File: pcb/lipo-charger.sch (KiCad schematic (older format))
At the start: 15 parts, among them J101 Barrel_Jack, J102 Conn_01x04, J103 Conn_01x03, J104 Conn_01x03, P101 Polarity, P102 Outline, P103 OSHW, U101 LM317L_TO92

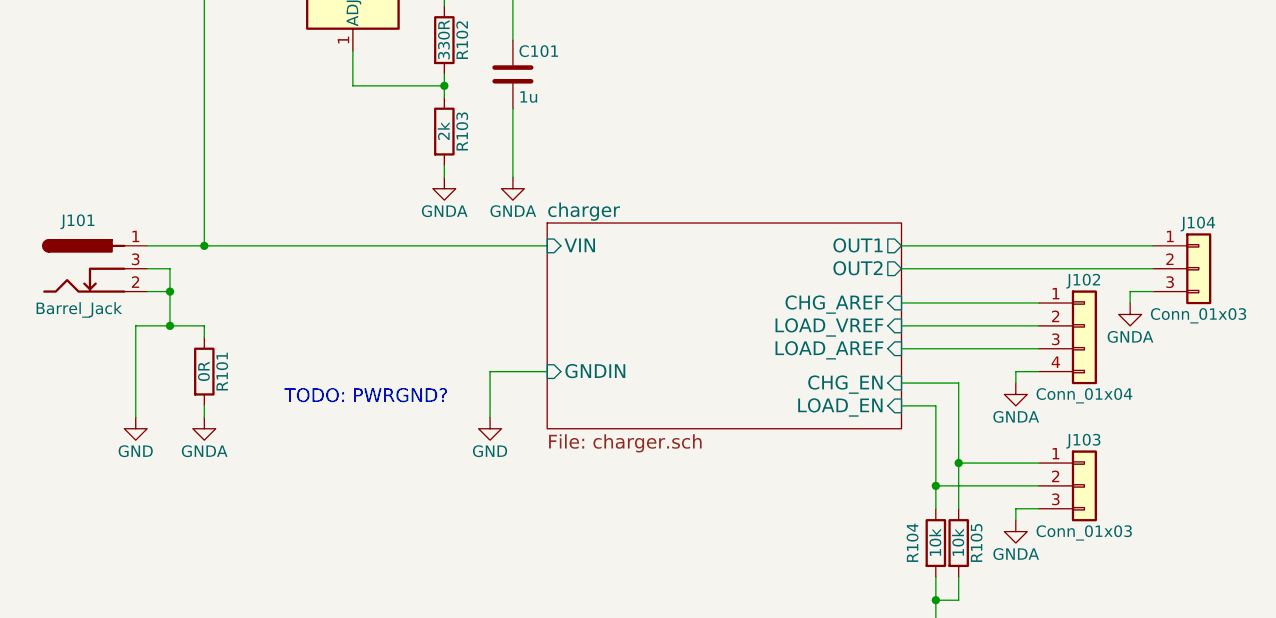
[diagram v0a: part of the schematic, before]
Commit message: Fix ERC/DRC errors for first prototype
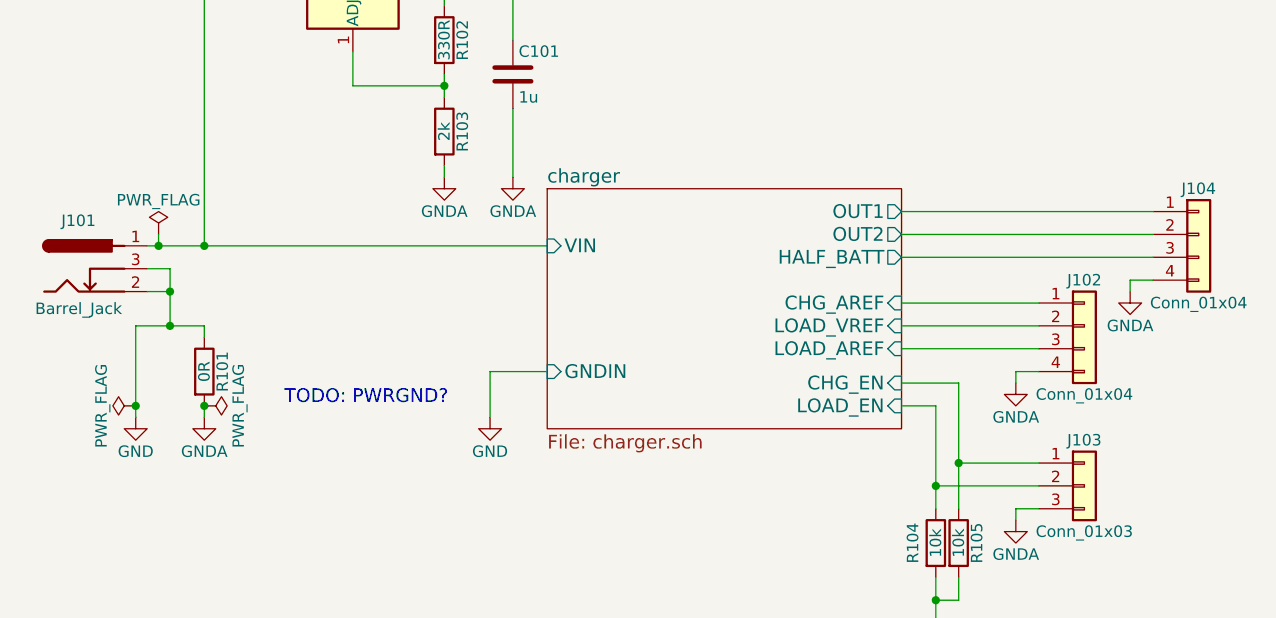
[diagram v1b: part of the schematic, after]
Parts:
- removed J104: Conn_01x03, Pin_Headers:Pin_Header_Straight_1x03_Pitch2.54mm, symbol Conn_01x03
- added J104: Conn_01x04, Pin_Headers:Pin_Header_Straight_1x04_Pitch2.54mm, symbol Conn_01x04
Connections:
- net GNDA: now also J104.4 (Pin_4)
- net charger/OUT1: now also J104.1 (Pin_1)
- net charger/OUT2: now also J104.2 (Pin_2)
- new net charger/HALF_BATT: J104.3 (Pin_3)
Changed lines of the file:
@@
 $EndComp
 $Sheet
-S 5300 2000 1550 900
+S 5300 1850 1550 1050
 U 5A337ADE
 F0 "charger" 60
@@
 F6 "LOAD_VREF" I R 6850 2450 60
 F7 "GNDIN" I L 5300 2650 60
-F8 "OUT1" O R 6850 2100 60
-F9 "OUT2" O R 6850 2200 60
+F8 "OUT1" O R 6850 1950 60
+F9 "OUT2" O R 6850 2050 60
 F10 "LOAD_EN" I R 6850 2800 60
+F11 "HALF_BATT" O R 6850 2150 60
 $EndSheet
 $Comp
@@
 Wire Wire Line
 	5150 900  5150 1200
-$Comp
-L Conn_01x03 J104
-U 1 1 5A3CE784
-P 8150 2200
-F 0 "J104" H 8150 2400 50  0000 C CNN
-F 1 "Conn_01x03" H 8150 2000 50  0000 C CNN
-F 2 "Pin_Headers:Pin_Header_Straight_1x03_Pitch2.54mm" H 8150 2200 50  0001 C CNN
-F 3 "" H 8150 2200 50  0001 C CNN
-	1    8150 2200
-	1    0    0    -1
-$EndComp
-Wire Wire Line
-	7950 2100 6850 2100
-Wire Wire Line
-	6850 2200 7950 2200
+Wire Wire Line
+	7950 1950 6850 1950
+Wire Wire Line
+	6850 2050 7950 2050
 $Comp
 L GNDA #PWR06
 U 1 1 5A3CE8B0
-P 7850 2350
-F 0 "#PWR06" H 7850 2100 50  0001 C CNN
-F 1 "GNDA" H 7850 2200 50  0000 C CNN
-F 2 "" H 7850 2350 50  0001 C CNN
-F 3 "" H 7850 2350 50  0001 C CNN
-	1    7850 2350
-	1    0    0    -1
-$EndComp
-Wire Wire Line
-	7950 2300 7850 2300
-Wire Wire Line
-	7850 2300 7850 2350
+P 7850 2300
+F 0 "#PWR06" H 7850 2050 50  0001 C CNN
+F 1 "GNDA" H 7850 2150 50  0000 C CNN
+F 2 "" H 7850 2300 50  0001 C CNN
+F 3 "" H 7850 2300 50  0001 C CNN
+	1    7850 2300
+	1    0    0    -1
+$EndComp
+Wire Wire Line
+	7950 2250 7850 2250
+Wire Wire Line
+	7850 2250 7850 2300
 $Comp
 L Conn_01x04 J102
@@
 	1    0    0    -1
 $EndComp
+$Comp
+L Conn_01x04 J104
+U 1 1 5A3D7236
+P 8150 2050
+F 0 "J104" H 8150 2250 50  0000 C CNN
+F 1 "Conn_01x04" H 8150 1750 50  0000 C CNN
+F 2 "Pin_Headers:Pin_Header_Straight_1x04_Pitch2.54mm" H 8150 2050 50  0001 C CNN
+F 3 "" H 8150 2050 50  0001 C CNN
+	1    8150 2050
+	1    0    0    -1
+$EndComp
+Wire Wire Line
+	6850 2150 7950 2150
+$Comp
+L PWR_FLAG #FLG011
+U 1 1 5A3D7A81
+P 3500 2800
+F 0 "#FLG011" H 3500 2875 50  0001 C CNN
+F 1 "PWR_FLAG" H 3500 2950 50  0000 C CNN
+F 2 "" H 3500 2800 50  0001 C CNN
+F 3 "" H 3500 2800 50  0001 C CNN
+	1    3500 2800
+	0    -1   -1   0
+$EndComp
+$Comp
+L PWR_FLAG #FLG012
+U 1 1 5A3D7AFC
+P 3800 2800
+F 0 "#FLG012" H 3800 2875 50  0001 C CNN
+F 1 "PWR_FLAG" H 3800 2950 50  0000 C CNN
+F 2 "" H 3800 2800 50  0001 C CNN
+F 3 "" H 3800 2800 50  0001 C CNN
+	1    3800 2800
+	0    1    1    0
+$EndComp
+Connection ~ 3800 2800
+Connection ~ 3500 2800
+$Comp
+L PWR_FLAG #FLG013
+U 1 1 5A3D7BDD
+P 3600 2050
+F 0 "#FLG013" H 3600 2125 50  0001 C CNN
+F 1 "PWR_FLAG" H 3600 2200 50  0000 C CNN
+F 2 "" H 3600 2050 50  0001 C CNN
+F 3 "" H 3600 2050 50  0001 C CNN
+	1    3600 2050
+	1    0    0    -1
+$EndComp
+Wire Wire Line
+	3600 2050 3600 2100
+Connection ~ 3600 2100
 $EndSCHEMATC

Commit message: Massive rework, fully routed
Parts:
- removed C101: 1u, Capacitors_SMD_Round:C_0805, symbol C
- removed J101: Barrel_Jack, Connectors:Barrel_Jack_CUI_PJ-102AH, symbol Barrel_Jack
- removed J103: Conn_01x03, Pin_Headers:Pin_Header_Straight_1x03_Pitch2.54mm, symbol Conn_01x03
- removed J104: Conn_01x04, Pin_Headers:Pin_Header_Straight_1x04_Pitch2.54mm, symbol Conn_01x04
- removed P101: Polarity, Polarity_Symbols:Polarity_Center_Positive_3mm_SilkScreen, symbol SYMBOL
- removed R102: 330R, Resistors_SMD:R_0603_HandSoldering, symbol R
- removed R103: 2k, Resistors_SMD:R_0603_HandSoldering, symbol R
- removed R104, R105: 10k, Resistors_SMD:R_0603_HandSoldering, symbol R
- removed TP101: TEST, Measurement_Points:Measurement_Point_Round-SMD-Pad_Small, symbol TEST
- removed U101: LM317L_TO92, TO_SOT_Packages_THT:TO-92_Inline_Narrow_Oval, symbol LM317L_TO92
- added J101, J103: Conn_01x04, Connectors_Molex:Molex_KK-6410-04_04x2.54mm_Straight, symbol Conn_01x04
- added J104: Conn_01x03, Connectors_Molex:Molex_KK-6410-03_03x2.54mm_Straight, symbol Conn_01x03
- added P? (x2): Fid, Fiducials:Fiducial_1mm_Dia_2.54mm_Outer_CopperTop, symbol SYMBOL
- J102: footprint Pin_Headers:Pin_Header_Straight_1x04_Pitch2.54mm -> Connectors_Molex:Molex_KK-6410-04_04x2.54mm_Straight
- R101: value 0R -> 100R
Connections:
- net +9VA: now also J102.1 (Pin_1)
- net GNDA: now also J102.2 (Pin_2), J101.4 (Pin_4), J103.4 (Pin_4), J104.3 (Pin_3); no longer J102.4 (Pin_4)
- net charger/CHG_AREF: now also J101.2 (Pin_2); no longer J102.1 (Pin_1)
- net charger/CHG_EN: now also J101.1 (Pin_1)
- net charger/LOAD_AREF: now also J103.3 (Pin_3); no longer J102.3 (Pin_3)
- net charger/LOAD_EN: now also J103.1 (Pin_1)
- net charger/LOAD_VREF: now also J103.2 (Pin_2); no longer J102.2 (Pin_2)
- net charger/OUT1: now also J104.1 (Pin_1)
- net charger/OUT2: now also J104.2 (Pin_2)
- net charger/VIN: now also J102.3 (Pin_3)
- net GND renamed charger/GNDIN
- net charger/GNDIN: now also J102.4 (Pin_4)
- new net charger/MASTER_EN: J101.3 (Pin_3)
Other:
- note added: "Note: R101 is optional\ntie between grounds"
- note added: "This is a dev board which might\nbecome a module in a larger\ncharger apparatus."
- note removed: "TODO: PWRGND?"

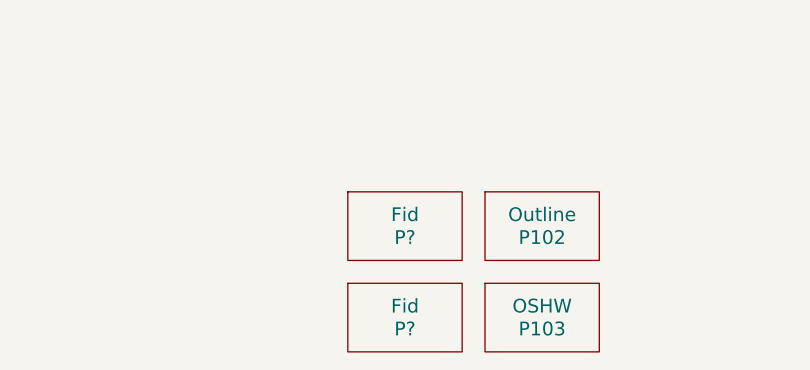
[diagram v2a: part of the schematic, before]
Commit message: Rename some nets, ordered.
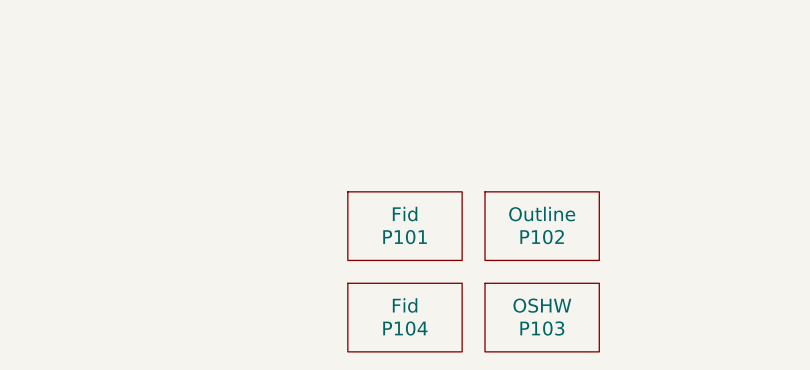
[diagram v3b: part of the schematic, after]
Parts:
- gave numbers to parts that had none: 2
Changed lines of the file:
@@
 	5100 2800 5100 3250
 $Comp
-L +9VA #PWR01
+L +9VA #PWR101
 U 1 1 5A473903
 P 5100 2800
-F 0 "#PWR01" H 5100 2675 50  0001 C CNN
+F 0 "#PWR101" H 5100 2675 50  0001 C CNN
 F 1 "+9VA" H 5100 2950 50  0000 C CNN
 F 2 "" H 5100 2800 50  0001 C CNN
@@
 $EndComp
 $Comp
-L GNDA #PWR02
+L GNDA #PWR103
 U 1 1 5A473953
 P 5600 3100
-F 0 "#PWR02" H 5600 2850 50  0001 C CNN
+F 0 "#PWR103" H 5600 2850 50  0001 C CNN
 F 1 "GNDA" H 5600 2950 50  0000 C CNN
 F 2 "" H 5600 3100 50  0001 C CNN
@@
 $EndComp
 $Comp
-L GNDA #PWR03
+L GNDA #PWR102
 U 1 1 5A4739A7
 P 5250 4600
-F 0 "#PWR03" H 5250 4350 50  0001 C CNN
+F 0 "#PWR102" H 5250 4350 50  0001 C CNN
 F 1 "GNDA" H 5250 4450 50  0000 C CNN
 F 2 "" H 5250 4600 50  0001 C CNN
@@
 $EndComp
 $Comp
-L PWR_FLAG #FLG04
+L PWR_FLAG #FLG102
 U 1 1 5A473E6C
 P 5550 3050
-F 0 "#FLG04" H 5550 3125 50  0001 C CNN
+F 0 "#FLG102" H 5550 3125 50  0001 C CNN
 F 1 "PWR_FLAG" H 5550 3200 50  0000 C CNN
 F 2 "" H 5550 3050 50  0001 C CNN
@@
 Connection ~ 5550 3100
 $Comp
-L PWR_FLAG #FLG05
+L PWR_FLAG #FLG101
 U 1 1 5A473EF3
 P 5100 2900
-F 0 "#FLG05" H 5100 2975 50  0001 C CNN
+F 0 "#FLG101" H 5100 2975 50  0001 C CNN
 F 1 "PWR_FLAG" H 5100 3050 50  0000 C CNN
 F 2 "" H 5100 2900 50  0001 C CNN
@@
 This is a dev board which might\nbecome a module in a larger\ncharger apparatus.
 $Comp
-L SYMBOL P?
+L SYMBOL P101
 U 1 1 5A4800FD
 P 5900 7100
-F 0 "P?" H 5900 7050 60  0000 C CNN
+F 0 "P101" H 5900 7050 60  0000 C CNN
 F 1 "Fid" H 5900 7150 60  0000 C CNN
 F 2 "Fiducials:Fiducial_1mm_Dia_2.54mm_Outer_CopperTop" H 5900 7100 60  0001 C CNN
@@
 $EndComp
 $Comp
-L SYMBOL P?
+L SYMBOL P104
 U 1 1 5A480219
 P 5900 7500
-F 0 "P?" H 5900 7450 60  0000 C CNN
+F 0 "P104" H 5900 7450 60  0000 C CNN
 F 1 "Fid" H 5900 7550 60  0000 C CNN
 F 2 "Fiducials:Fiducial_1mm_Dia_2.54mm_Outer_CopperTop" H 5900 7500 60  0001 C CNN
